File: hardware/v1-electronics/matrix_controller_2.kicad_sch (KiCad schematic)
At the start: 13 parts, among them IC4 IS31FL3733-QFLS4-TR

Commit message: checkpoint(v1 hardware): this is the save before corrections
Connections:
- net VDD renamed V_REG0
- net V_SYS renamed +5V
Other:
- title: (none) -> Slack
- moved on the sheet: IC4

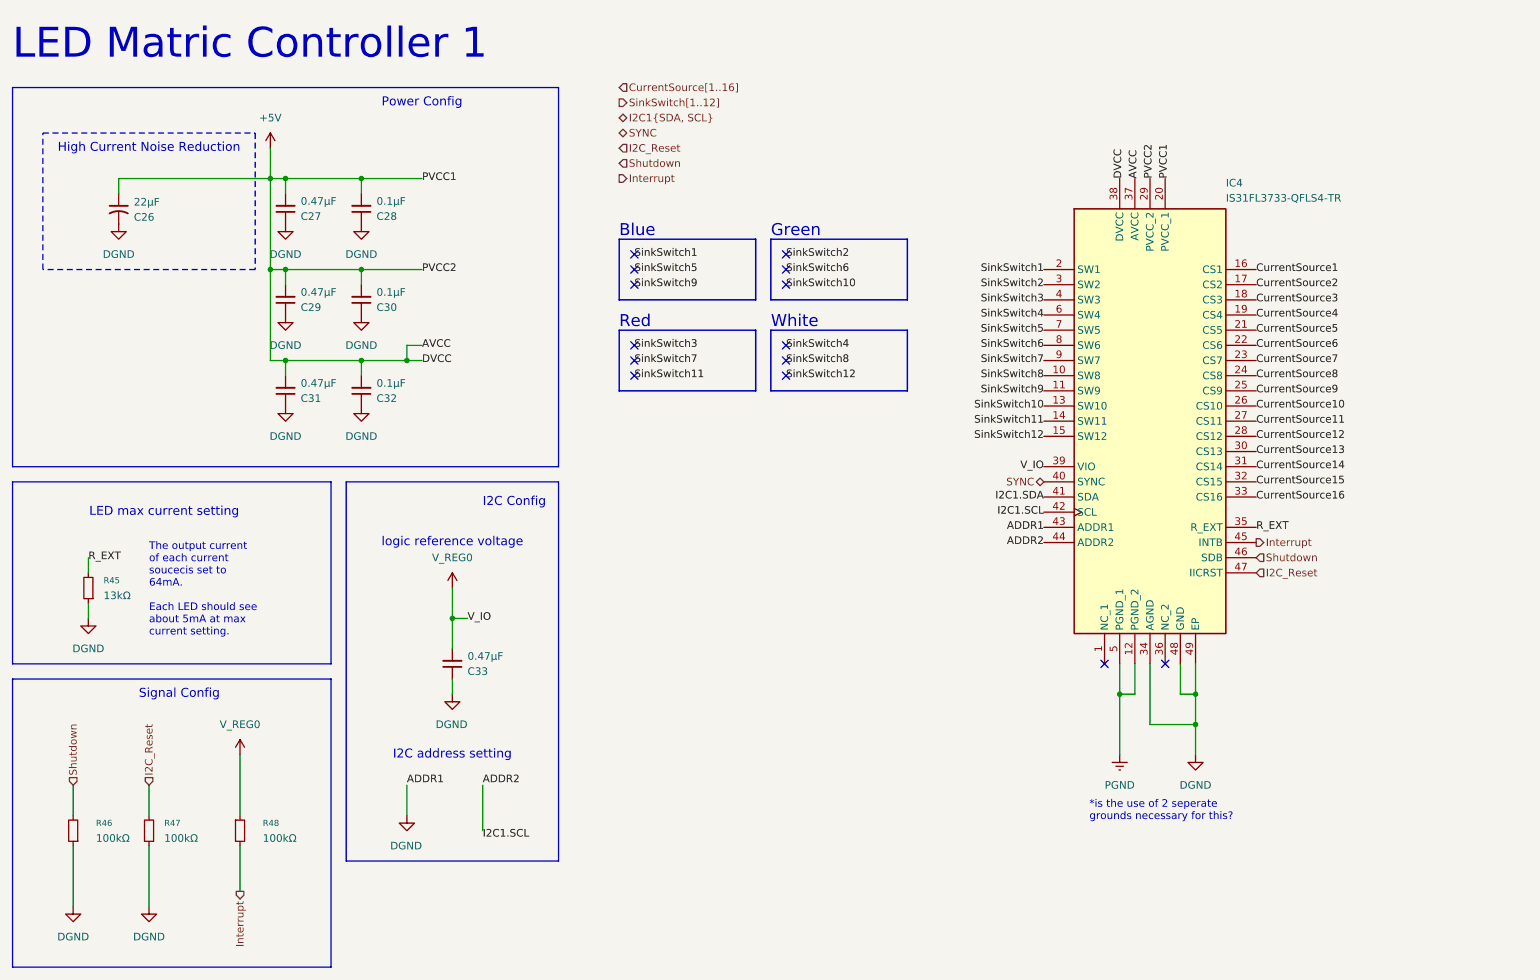
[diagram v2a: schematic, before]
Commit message: fix(v1 hardware): complete set of recommendations
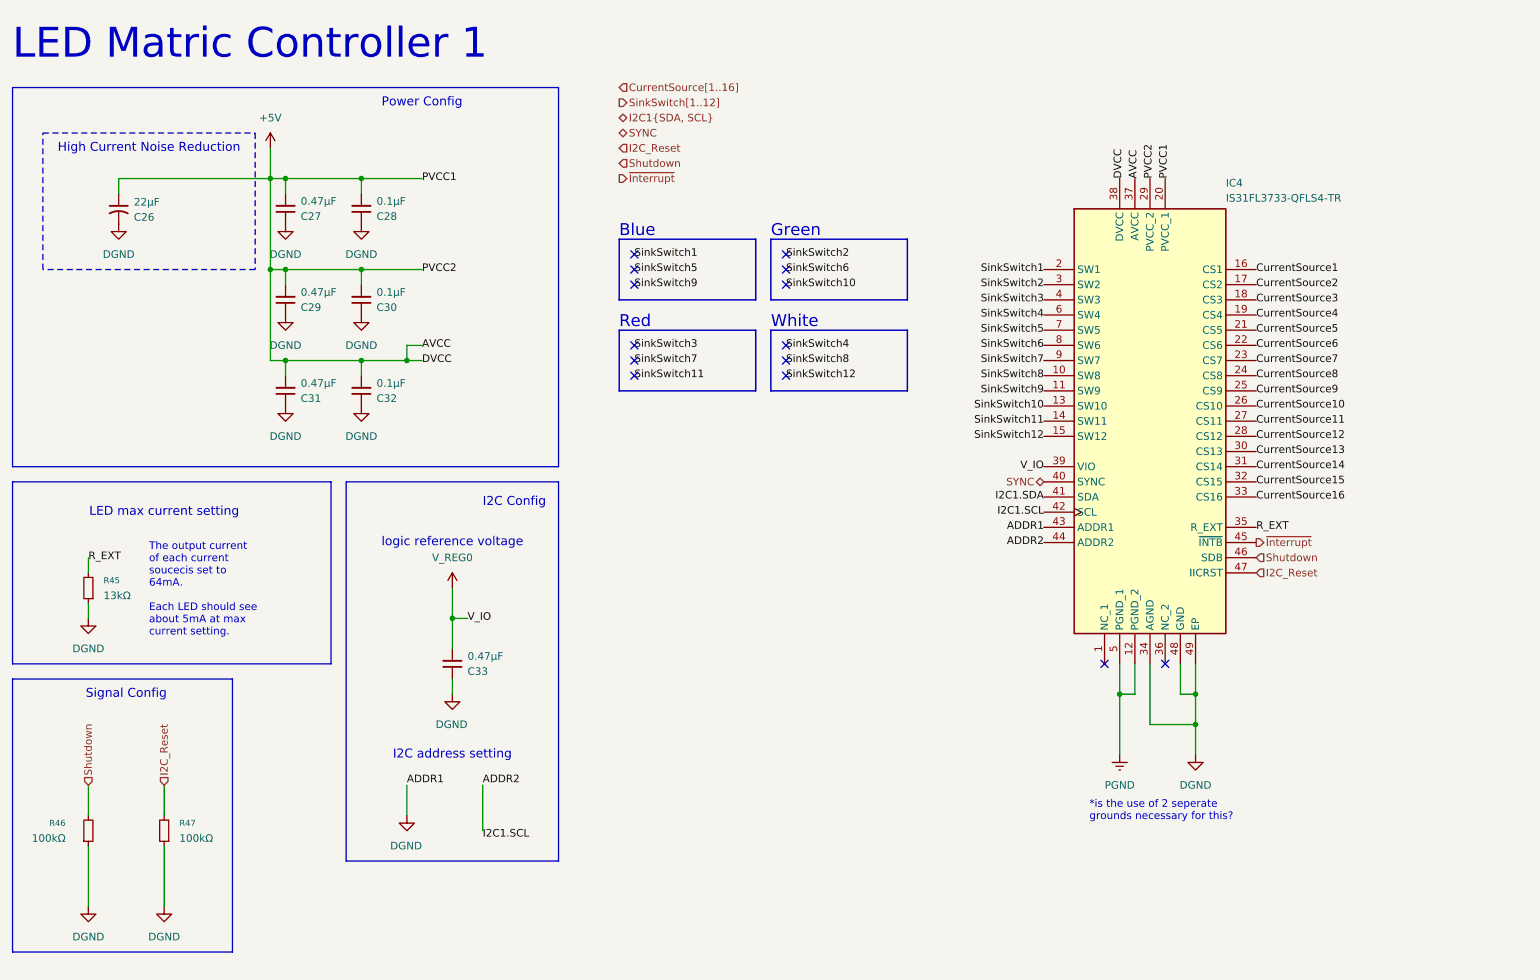
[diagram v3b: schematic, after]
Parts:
- removed R48: 100kΩ, symbol Device:R_Small
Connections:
- net Interrupt renamed ~{Interrupt}
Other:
- moved on the sheet: R46, R47

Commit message: feat(v1 hardware): place foot prints
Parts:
- C26: footprint (none) -> Capacitor_Tantalum_SMD:CP_EIA-3216-18_Kemet-A; symbol Device:C_Small_US -> Device:C_Polarized_Small
- C27, C29, C31, C33: footprint (none) -> Capacitor_SMD:C_0805_2012Metric
- C28, C30, C32: footprint (none) -> Capacitor_SMD:C_0402_1005Metric
- IC4: footprint QFN40P600X600X80-49N-D -> Lumissil Microsystems:QFN40P600X600X80-49N-D
- R45: footprint (none) -> Resistor_SMD:R_0201_0603Metric
- R46, R47: footprint (none) -> Resistor_SMD:R_0805_2012Metric

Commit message: feat(v1 hardware): review fixes
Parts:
- R45: value 13kΩ -> 22kΩ
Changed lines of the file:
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@@
 			)
 		)
-		(property "Value" "13kΩ"
+		(property "Value" "22kΩ"
 			(at 30.48 110.4899 0)
 			(show_name no)
@@
 			)
 		)
-		(property "Description" "part selected: 0603WAF1302T5E"
+		(property "Description" "part selected: 0603WAF2202T5E"
 			(at 27.94 109.22 0)
 			(hide yes)
